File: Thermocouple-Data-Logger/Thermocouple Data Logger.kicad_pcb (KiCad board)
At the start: 4 copper layers, 75 x 85 mm, 149 parts, among them J0 Power, J1 Micro_SD_Card_Det, J2 Probe 1, J3 Probe 2, J4 Probe 3, J5 Probe 4, J6 ISP, SW0 Power, SW1 Display, SW2 Reset, SW3 Select/Calibrate, SW4 Cycle/Menu, SW5 SW_DIP_x04, U0 ATMEGA324PA-MU, U1 LT1763-3.3, U10 74HC595, U11 HDSP-521E-Display, U12 HDSP-521E-Display, U13 4050, U2 MAX31856, U3 MAX31856, U4 MAX31856, U5 MAX31856, U6 74HC595, U7 74HC595, U8 74HC595, U9 74HC595, Y0 10MHz, Y1 32.768KHz

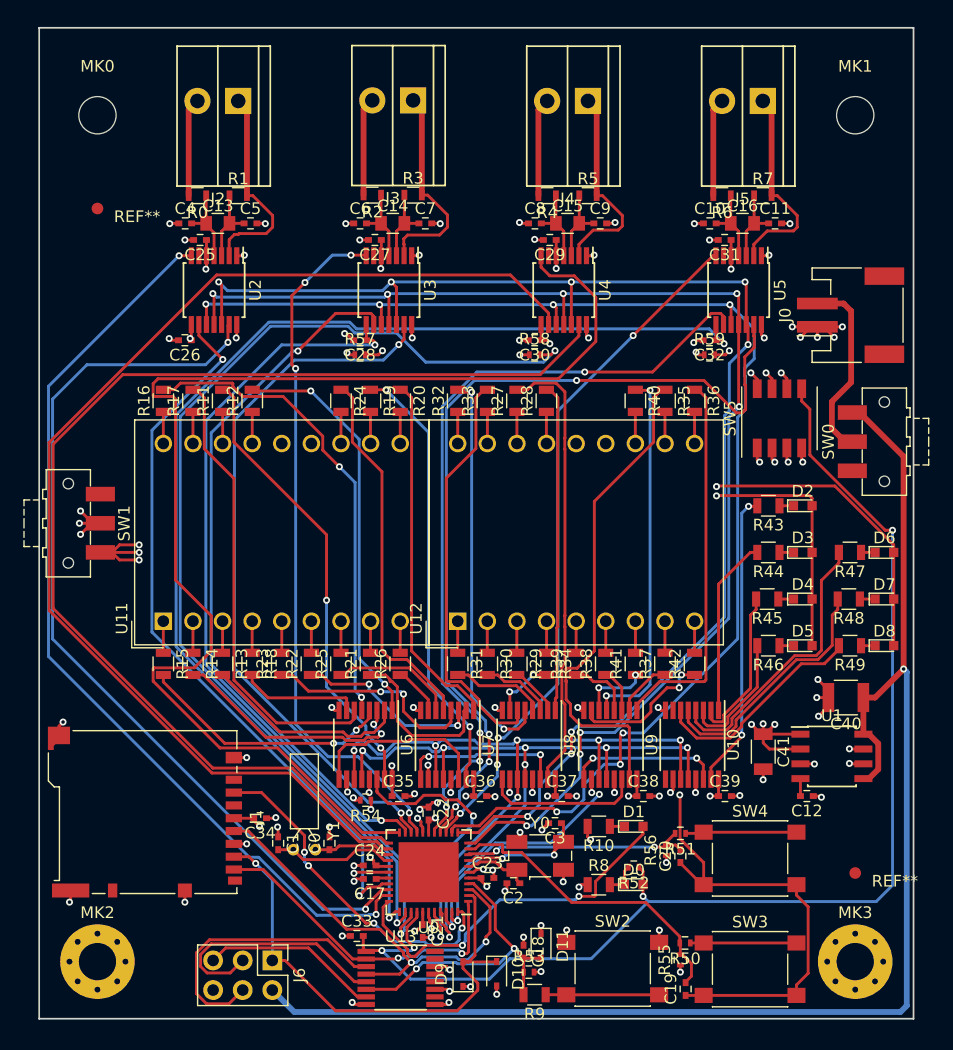
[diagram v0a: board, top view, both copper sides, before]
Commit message: Satrted Labling the Components
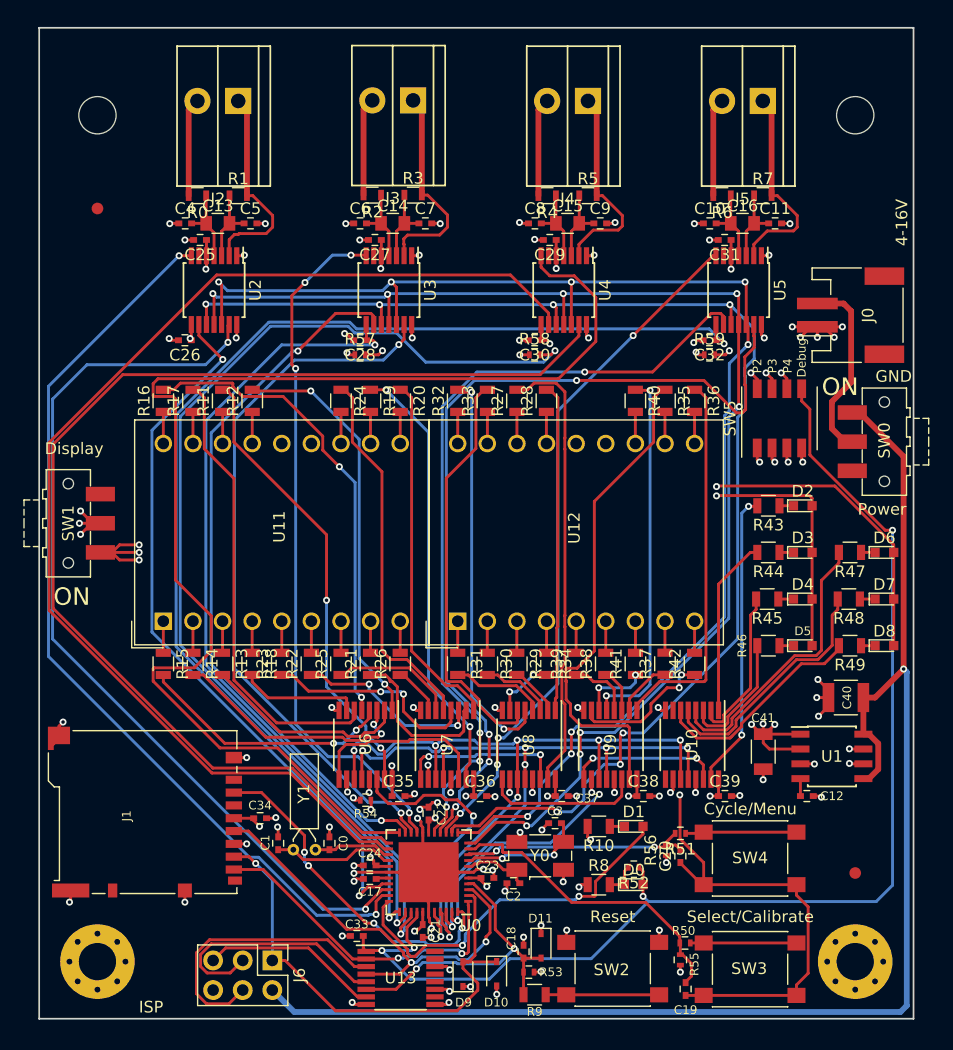
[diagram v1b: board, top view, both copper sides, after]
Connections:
- U0 pad 45: (no net) -> GND
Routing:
- net GND: track 120.4 -> 141.3 mm
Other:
- board text added: "4-16V"
- board text added: "Debug"
- board text added: "GND"
- board text added: "ON"
- board text added: "P2"
- board text added: "P3"
- board text added: "P4"
- board text added: "Termocouple Data Logger - Rev 1 (c) 2018 Corwin Hansen corwinh.com https://github.com/ch98-1/Thermocouple-Data-Logger"

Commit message: Finished labling the board. Ver 1 hardware
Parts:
- added REF***: OSHW-Logo_11.4x12mm_SilkScreen, Symbols:OSHW-Logo_11.4x12mm_SilkScreen, B.Cu at (118.3, 115.3)
- moved D7 0.10 mm to (181.4, 98.0)
- moved D4 0.10 mm to (174.4, 98.0)
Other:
- board text added: "+"
- board text added: "-"
- board text added: "K"
- board text added: "Probe 1"
- board text added: "Probe 2"
- board text added: "Probe 3"
- board text added: "Probe 4"
- board text added: "°C"
- board text added: "°F"
